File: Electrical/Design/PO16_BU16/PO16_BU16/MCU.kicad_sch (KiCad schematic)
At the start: 32 parts, among them J2 (NF), SW1 C255807, U7 SAMD51N20A, U8 W25Q16JVSSIQ

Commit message: SUKU PO16_BU16 workflow files updated for v6 MAN-36
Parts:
- LOGO1: value (none) -> OSHWA; footprint (none) -> suku_basics:OSHWA
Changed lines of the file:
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@@
       (effects (font (size 1.27 1.27)) hide)
     )
-    (property "Value" "" (id 1) (at 396.24 247.015 0)
+    (property "Value" "OSHWA" (id 1) (at 396.24 247.015 0)
       (effects (font (size 1.27 1.27)) hide)
     )
-    (property "Footprint" "" (id 2) (at 396.24 241.3 0)
+    (property "Footprint" "suku_basics:OSHWA" (id 2) (at 396.24 241.3 0)
       (effects (font (size 1.27 1.27)) hide)
     )

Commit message: SUKU po16_bu16 cloned from pbf4
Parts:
- removed C38, C43: 10u, suku_basics:CAP_0805, symbol suku_basics:CAP
- removed C39, C41, C42, C44, C45, C46, C47, C48, C49, C54, C55: 100n, suku_basics:CAP_0805, symbol suku_basics:CAP
- removed C40: 1u, suku_basics:CAP_0805, symbol suku_basics:CAP
- removed J2: (NF), Connector_PinHeader_1.27mm:PinHeader_2x05_P1.27mm_Vertical, symbol Connector_Generic:Conn_02x05_Odd_Even
- removed L1: GZ2012D601TF, suku_basics:FERRIT_0805, symbol suku_basics:FERRIT
- removed LOGO1: OSHWA, suku_basics:OSHWA, symbol suku_basics:OSHWA
- removed R38, R39, R41, R42: 1k, suku_basics:RES_0805, symbol suku_basics:RES
- removed R43: 5k1, suku_basics:RES_0805, symbol suku_basics:RES
- removed TP1, TP2, TP3, TP4: TestPoint, TestPoint:TestPoint_THTPad_1.0x1.0mm_Drill0.5mm, symbol Connector:TestPoint
- removed U7: SAMD51N20A, suku_basics:TQFP-100_14x14mm_P0.5mm, symbol suku_basics:SAMD51N20A
- added C731, C732, C735, C736, C737, C738, C740, C741, C744, C745, C747, C749, C751, C752: 100n, suku_basics:CAP_0402, symbol suku_basics:CAP
- added C733, C734, C746, C754, C755, C758: 1u, suku_basics:CAP_0402, symbol suku_basics:CAP
- added C739: 3p9, suku_basics:CAP_0402, symbol suku_basics:CAP
- added C742: 1p8, suku_basics:CAP_0402, symbol suku_basics:CAP
- added C743: 10u, suku_basics:CAP_0402, symbol suku_basics:CAP
- added C748, C750: 10p, suku_basics:CAP_0402, symbol suku_basics:CAP
- added C753: 10n, suku_basics:CAP_0402, symbol suku_basics:CAP
- added J701: Conn_Coaxial, Connector_Coaxial:U.FL_Molex_MCRF_73412-0110_Vertical, symbol Connector:Conn_Coaxial
- added J702: (NF), Connector_PinHeader_1.27mm:PinHeader_2x05_P1.27mm_Vertical, symbol Connector_Generic:Conn_02x05_Odd_Even
- added L701: 1n8, suku_basics:IND_0402, symbol suku_basics:INDUCTOR
- added L702: GZ2012D601TF, suku_basics:FERRIT_0805, symbol suku_basics:FERRIT
- added LOGO701: OSHWA, suku_basics:OSHWA, symbol suku_basics:OSHWA
- added R729, R732, R734, R735: 5k1, suku_basics:RES_0402, symbol suku_basics:RES
- added R733: 1k, suku_basics:RES_0402, symbol suku_basics:RES
- added SW702, SW703: C2905169, Button_Switch_SMD:SW_SPST_CK_RS282G05A3, symbol Switch:SW_SPST
- added TP701, TP702, TP703, TP704, TP706, TP707, TP708, TP709: TestPoint, TestPoint:TestPoint_Pad_D1.0mm, symbol Connector:TestPoint
- added TP705, TP710: TestPoint, TestPoint:TestPoint_Pad_1.0x1.0mm, symbol Connector:TestPoint
- added U703: RP2040, suku_basics:RP2040_QFN-56-1EP_7x7mm_P0.4mm_EP3.2x3.2mm, symbol suku_basics:RP2040
- added U704: ESP32-S3FN8, suku_basics:QFN-56-1EP_7x7mm_P0.4mm_EP3.2x3.2mm, symbol suku_basics:ESP32-S3FN8
- added Y701: ESP32_XTAL, Crystal:Crystal_SMD_Abracon_ABM8G-4Pin_3.2x2.5mm, symbol suku_basics:ESP32_XTAL
- C756: renamed from C56; footprint suku_basics:CAP_0805 -> suku_basics:CAP_0402
- C757: renamed from C57; footprint suku_basics:CAP_0805 -> suku_basics:CAP_0402
- R736: renamed from R40; footprint suku_basics:RES_0805 -> suku_basics:RES_0402
- U705: renamed from U8; value W25Q16JVSSIQ -> W25Q64JVSSIQ
- renumbered SW1 to SW701
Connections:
- net GND: now also C731.2, C732.2, C733.2, C734.2, C735.2, C736.2, C737.2, C738.2, C739.2, C740.2, C741.2, C742.2, C743.2, C744.2, C745.2, C746.2, C747.2, C748.2, C749.2, C750.2, C751.2, C752.2, C753.2, C754.2, C755.2, C758.2, J701.2 (Ext), J702.5 (Pin_5), SW702.1 (A), SW703.1 (A), TP705.1, TP710.1, U703.19 (TESTEN), U703.57 (GND), U704.57 (GND), Y701.2, Y701.4; no longer C757.2
- net GRID_EAST_RX: now also U703.36 (GPIO24)
- net GRID_EAST_TX: now also U703.38 (GPIO26_ADC0)
- net GRID_NORTH_RX: now also U703.8 (GPIO6)
- net GRID_NORTH_TX: now also U703.35 (GPIO23)
- net GRID_SOUTH_RX: now also U703.39 (GPIO27_ADC1)
- net GRID_SOUTH_TX: now also U703.4 (GPIO2)
- net GRID_SYNC_1: now also U703.37 (GPIO25)
- net GRID_SYNC_2: now also U703.6 (GPIO4)
- net GRID_WEST_RX: now also U703.5 (GPIO3)
- net GRID_WEST_TX: now also U703.7 (GPIO5)
- net HWCFG_CLOCK: now also U704.16 (GPIO11)
- net HWCFG_DATA: now also U704.17 (GPIO12)
- net HWCFG_SHIFT: now also U704.15 (GPIO10)
- net LED_DATA_OUT: now also U704.27 (GPIO21)
- net MAP_MODE: now also U704.43 (GPIO38)
- net USB_DN: now also U704.25 (GPIO19)
- net USB_DP: now also U704.26 (GPIO20)
- net +3V3_UC renamed VDD_SPI
- net VDD_SPI: now also C755.1, R734.1, U704.29 (VDD_SPI)
- net QSPI_IO_0 renamed SPID
- net SPID: now also U704.35 (GPIO32)
- net QSPI_IO_1 renamed SPIQ
- net SPIQ: now also U704.34 (GPIO31)
- net QSPI_IO_2 renamed SPIWP
- net SPIWP: now also U704.31 (GPIO28)
- net QSPI_IO_3 renamed SPIHD
- net SPIHD: now also U704.30 (GPIO27)
- net QSPI_SCK renamed SPICLK
- net SPICLK: now also U704.33 (GPIO30)
- net QSPI_~{CE} renamed SPICS0
- net SPICS0: now also R734.2, U704.32 (GPIO29)
- new net: TP704.1, U703.18 (GPIO15)
- new net: TP701.1, U703.15 (GPIO12)
- new net: TP702.1, U703.16 (GPIO13)
- new net: TP703.1, U703.17 (GPIO14)
- new net: C749.1, L702.1, U704.2 (VDD3P3), U704.3 (VDD3P3)
- new net: C739.1, J701.1 (In), L701.1
- new net: C750.1, U704.53 (XTAL_N), Y701.3
- new net: C748.1, U704.54 (XTAL_P), Y701.1
- new net: J702.7 (Pin_7), R733.1
- new net: R732.2, R735.1
- new net +1V1: C731.1, C732.1, C733.1, U703.23 (DVDD), U703.45 (VREG_VOUT), U703.50 (DVDD)
- new net +3V3: C734.1, C735.1, C736.1, C737.1, C738.1, C740.1, C741.1, C743.1, C744.1, C745.1, C746.1, C747.1, C751.1, C752.1, C753.1, C754.1, C757.2, L702.2, R729.1, R732.1, U703.1 (IOVDD), U703.10 (IOVDD), U703.22 (IOVDD), U703.33 (IOVDD), U703.42 (IOVDD), U703.43 (ADC_AVDD), U703.44 (VREG_IN), U703.48 (USB_VDD), U703.49 (IOVDD), U704.20 (VDD3P3_RTC), U704.46 (VDD3P3_CPU), U704.55 (VDDA1), U704.56 (VDDA2)
- new net ESP_BOOT0: SW703.2 (B), U704.5 (GPIO0)
- new net ESP_GPIO_1: U704.6 (GPIO1)
- new net ESP_GPIO_16: U704.22 (GPIO16)
- new net ESP_GPIO_18: U704.24 (GPIO18)
- new net ESP_GPIO_2: U704.7 (GPIO2)
- new net ESP_GPIO_3: U704.8 (GPIO3)
- new net ESP_GPIO_33: TP709.1, U704.38 (GPIO33)
- new net ESP_GPIO_34: TP708.1, U704.39 (GPIO34)
- new net ESP_GPIO_35: U704.40 (GPIO35)
- new net ESP_GPIO_36: U704.41 (GPIO36)
- new net ESP_GPIO_37: U704.42 (GPIO37)
- new net ESP_GPIO_4: U704.9 (GPIO4)
- new net ESP_GPIO_45: U704.51 (GPIO45)
- new net ESP_GPIO_46: U704.52 (GPIO46)
- new net ESP_GPIO_47: TP706.1, U704.37 (GPIO47)
- new net ESP_GPIO_48: TP707.1, U704.36 (GPIO48)
- new net ESP_GPIO_5: U704.10 (GPIO5)
- new net ESP_LNA: C742.1, L701.2, U704.1 (LNA_IN)
- new net ESP_RESET: C758.1, R735.2, SW702.2 (B), U704.4 (CHIP_PU)
- new net RP_CLK: U703.20 (XIN), U704.21 (GPIO15)
- new net RP_INTERRUPT: U703.34 (GPIO22), U704.23 (GPIO17)
- new net RP_RUN: R729.2, U703.26 (RUN)
- new net RP_SPI0_CS: U703.28 (GPIO17), U704.12 (GPIO7)
- new net RP_SPI0_RX: U703.27 (GPIO16), U704.11 (GPIO6)
- new net RP_SPI0_SCK: U703.29 (GPIO18), U704.14 (GPIO9)
- new net RP_SPI0_TX: U703.30 (GPIO19), U704.13 (GPIO8)
- new net RP_SWCLK: U703.24 (SWCLK), U704.19 (GPIO14)
- new net RP_SWDIO: U703.25 (SWD), U704.18 (GPIO13)
- new net RP_UART0_RX: J702.3 (Pin_3), U703.3 (GPIO1)
- new net RP_UART0_TX: J702.1 (Pin_1), U703.2 (GPIO0)
- new net TCK: J702.4 (Pin_4), U704.44 (GPIO39)
- new net TDI: J702.8 (Pin_8), U704.47 (GPIO41)
- new net TDO: J702.6 (Pin_6), U704.45 (GPIO40)
- new net TMS: J702.2 (Pin_2), U704.48 (GPIO42)
- new net U0RXD: J702.9 (Pin_9), U704.50 (GPIO44)
- new net U0TXD: R733.2, U704.49 (GPIO43)
- no-connect marks 46 -> 20
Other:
- removed sheet Sheet60EED5DC
- added sheet Sheet60F06FE1 (USB_POWER.kicad_sch)
- note added: "1.8nH LQG15HS1N8S02D 3.9pF GJM1555C1H3R9WB01D 1.8pF GJM1555C1H1R8BB01D"
- note added: "700"
- note added: "LCSC: TXM40M0004322HBCEO00T S3240000091040JY"
- note added: "Programming Interface"
- note added: "U.FL-R-SMT-1(80)"
- note removed: "Programming Interface Atmel ICE programmer/debugger connects to this port during manufacturing to burn the USB bootloader. Note: SWO is optional!"
- note removed: "XTAL"
- note removed: "bonus caps"
- moved on the sheet: C756, C757, U705

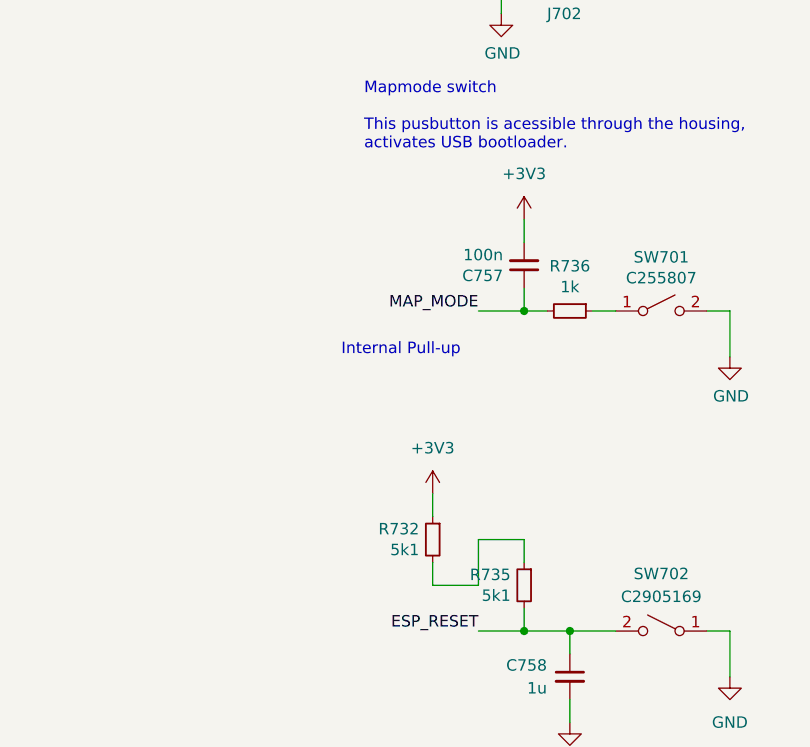
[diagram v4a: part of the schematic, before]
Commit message: SUKU via sizes and polygons updated
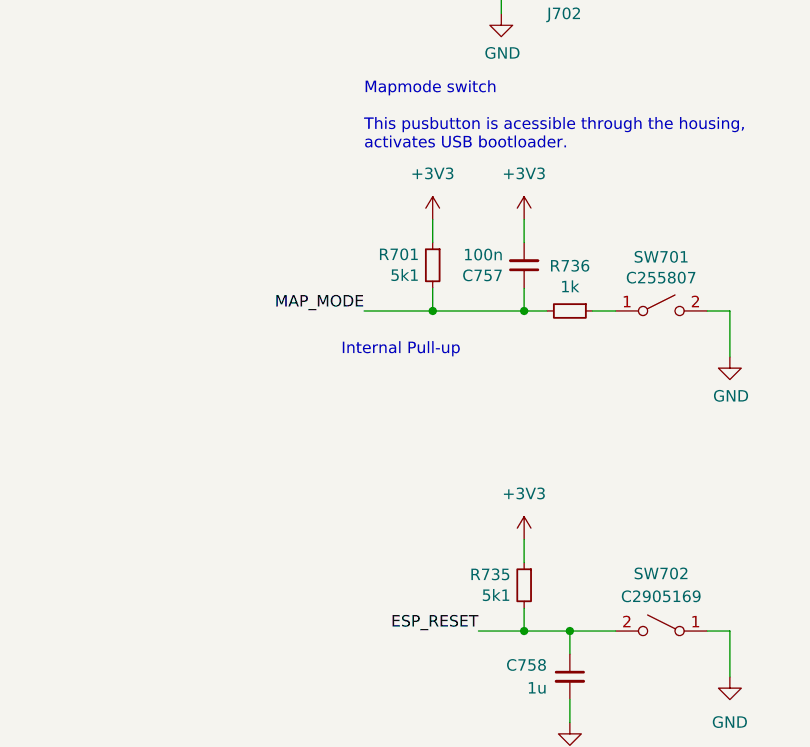
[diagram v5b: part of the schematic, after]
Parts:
- removed R732: 5k1, suku_basics:RES_0402, symbol suku_basics:RES
- added R701: 5k1, suku_basics:RES_0402, symbol suku_basics:RES
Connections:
- net +3V3: now also R735.1, R701.1
- net MAP_MODE: now also R701.2
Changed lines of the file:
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@@
   (junction (at 360.68 132.08) (diameter 0) (color 0 0 0 0)
   )
+  (junction (at 345.44 96.52) (diameter 0) (color 0 0 0 0)
+  )
   (junction (at 119.38 66.04) (diameter 0) (color 0 0 0 0)
   )
@@
     (stroke (width 0) (type default))
   )
-  (wire (pts (xy 350.52 127) (xy 350.52 121.92))
-    (stroke (width 0) (type default))
-  )
   (wire (pts (xy 154.94 218.44) (xy 152.4 218.44))
     (stroke (width 0) (type default))
@@
     (stroke (width 0) (type default))
   )
-  (wire (pts (xy 350.52 96.52) (xy 355.6 96.52))
+  (wire (pts (xy 337.82 96.52) (xy 345.44 96.52))
     (stroke (width 0) (type default))
   )
@@
     (stroke (width 0) (type default))
   )
+  (wire (pts (xy 345.44 93.98) (xy 345.44 96.52))
+    (stroke (width 0) (type default))
+  )
   (wire (pts (xy 350.52 231.14) (xy 350.52 233.68))
     (stroke (width 0) (type default))
@@
     (stroke (width 0) (type default))
   )
-  (wire (pts (xy 345.44 127) (xy 350.52 127))
-    (stroke (width 0) (type default))
-  )
   (wire (pts (xy 88.9 233.68) (xy 93.98 233.68))
     (stroke (width 0) (type default))
@@
     (stroke (width 0) (type default))
   )
-  (wire (pts (xy 345.44 116.84) (xy 345.44 119.38))
-    (stroke (width 0) (type default))
-  )
   (wire (pts (xy 27.94 185.42) (xy 27.94 187.96))
     (stroke (width 0) (type default))
@@
     (stroke (width 0) (type default))
   )
-  (wire (pts (xy 345.44 124.46) (xy 345.44 127))
-    (stroke (width 0) (type default))
-  )
   (wire (pts (xy 220.98 127) (xy 228.6 127))
     (stroke (width 0) (type default))
@@
     (stroke (width 0) (type default))
   )
+  (wire (pts (xy 345.44 96.52) (xy 355.6 96.52))
+    (stroke (width 0) (type default))
+  )
   (wire (pts (xy 154.94 248.92) (xy 152.4 248.92))
     (stroke (width 0) (type default))
@@
     (stroke (width 0) (type default))
   )
-  (wire (pts (xy 350.52 121.92) (xy 355.6 121.92))
-    (stroke (width 0) (type default))
-  )
   (wire (pts (xy 88.9 167.64) (xy 96.52 167.64))
     (stroke (width 0) (type default))
@@
     (stroke (width 0) (type default))
   )
+  (wire (pts (xy 345.44 86.36) (xy 345.44 88.9))
+    (stroke (width 0) (type default))
+  )
   (wire (pts (xy 134.62 35.56) (xy 134.62 38.1))
     (stroke (width 0) (type default))
@@
     (effects (font (size 1.27 1.27)) (justify right bottom))
   )
-  (label "MAP_MODE" (at 350.52 96.52 180) (fields_autoplaced)
+  (label "MAP_MODE" (at 337.82 96.52 180) (fields_autoplaced)
     (effects (font (size 1.27 1.27)) (justify right bottom))
   )
@@
     )
   )
-  (symbol (lib_id "power:+3V3") (at 345.44 116.84 0) (unit 1)
+  (symbol (lib_id "power:+3V3") (at 355.6 121.92 0) (unit 1)
     (in_bom yes) (on_board yes) (dnp no) (fields_autoplaced)
-    (property "Reference" "#PWR0835" (at 345.44 120.65 0)
+    (property "Reference" "#PWR0835" (at 355.6 125.73 0)
       (effects (font (size 1.27 1.27)) hide)
     )
-    (property "Value" "+3V3" (at 345.44 111.76 0)
+    (property "Value" "+3V3" (at 355.6 116.84 0)
       (effects (font (size 1.27 1.27)))
     )
-    (property "Footprint" "" (at 345.44 116.84 0)
+    (property "Footprint" "" (at 355.6 121.92 0)
       (effects (font (size 1.27 1.27)) hide)
     )
-    (property "Datasheet" "" (at 345.44 116.84 0)
+    (property "Datasheet" "" (at 355.6 121.92 0)
       (effects (font (size 1.27 1.27)) hide)
     )
@@
     )
   )
+  (symbol (lib_id "suku_basics:RES") (at 345.44 91.44 0) (mirror y) (unit 1)
+    (in_bom yes) (on_board yes) (dnp no)
+    (property "Reference" "R701" (at 343.9414 90.2716 0)
+      (effects (font (size 1.27 1.27)) (justify left))
+    )
+    (property "Value" "5k1" (at 343.9414 92.583 0)
+      (effects (font (size 1.27 1.27)) (justify left))
+    )
+    (property "Footprint" "suku_basics:RES_0402" (at 345.44 91.44 0)
+      (effects (font (size 1.27 1.27)) hide)
+    )
+    (property "Datasheet" "~" (at 345.44 91.44 0)
+      (effects (font (size 1.27 1.27)) hide)
+    )
+    (pin "1")
+    (pin "2")
+    (instances
+      (project "PO16_BU16"
+        (path "/e5217a0c-7f55-4c30-adda-7f8d95709d1b/00000000-0000-0000-0000-00005d757c78"
+          (reference "R701") (unit 1)
+        )
+      )
+    )
+  )
   (symbol (lib_id "power:+3V3") (at 355.6 86.36 0) (unit 1)
     (in_bom yes) (on_board yes) (dnp no) (fields_autoplaced)
@@
     )
   )
+  (symbol (lib_id "power:+3V3") (at 345.44 86.36 0) (unit 1)
+    (in_bom yes) (on_board yes) (dnp no) (fields_autoplaced)
+    (property "Reference" "#PWR01105" (at 345.44 90.17 0)
+      (effects (font (size 1.27 1.27)) hide)
+    )
+    (property "Value" "+3V3" (at 345.44 81.28 0)
+      (effects (font (size 1.27 1.27)))
+    )
+    (property "Footprint" "" (at 345.44 86.36 0)
+      (effects (font (size 1.27 1.27)) hide)
+    )
+    (property "Datasheet" "" (at 345.44 86.36 0)
+      (effects (font (size 1.27 1.27)) hide)
+    )
+    (pin "1")
+    (instances
+      (project "PO16_BU16"
+        (path "/e5217a0c-7f55-4c30-adda-7f8d95709d1b/00000000-0000-0000-0000-00005d757c78"
+          (reference "#PWR01105") (unit 1)
+        )
+      )
+    )
+  )
   (symbol (lib_id "suku_basics:CAP") (at 160.02 116.84 0) (unit 1)
     (in_bom yes) (on_board yes) (dnp no) (fields_autoplaced)
@@
         )
       )
-    )
-  )
-  (symbol (lib_id "suku_basics:RES") (at 345.44 121.92 0) (mirror y) (unit 1)
-    (in_bom yes) (on_board yes) (dnp no)
-    (property "Reference" "R732" (at 343.9414 120.7516 0)
-      (effects (font (size 1.27 1.27)) (justify left))
-    )
-    (property "Value" "5k1" (at 343.9414 123.063 0)
-      (effects (font (size 1.27 1.27)) (justify left))
-    )
-    (property "Footprint" "suku_basics:RES_0402" (at 345.44 121.92 0)
-      (effects (font (size 1.27 1.27)) hide)
-    )
-    (property "Datasheet" "~" (at 345.44 121.92 0)
-      (effects (font (size 1.27 1.27)) hide)
-    )
-    (pin "1")
-    (pin "2")
-    (instances
-      (project "PO16_BU16"
-        (path "/e5217a0c-7f55-4c30-adda-7f8d95709d1b/00000000-0000-0000-0000-00005d757c78"
-          (reference "R732") (unit 1)
-        )
-      )
